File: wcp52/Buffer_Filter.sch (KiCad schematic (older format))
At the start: 18 parts, among them Q10 MMBT3904, Q11 BFR540, Q12 BFR540

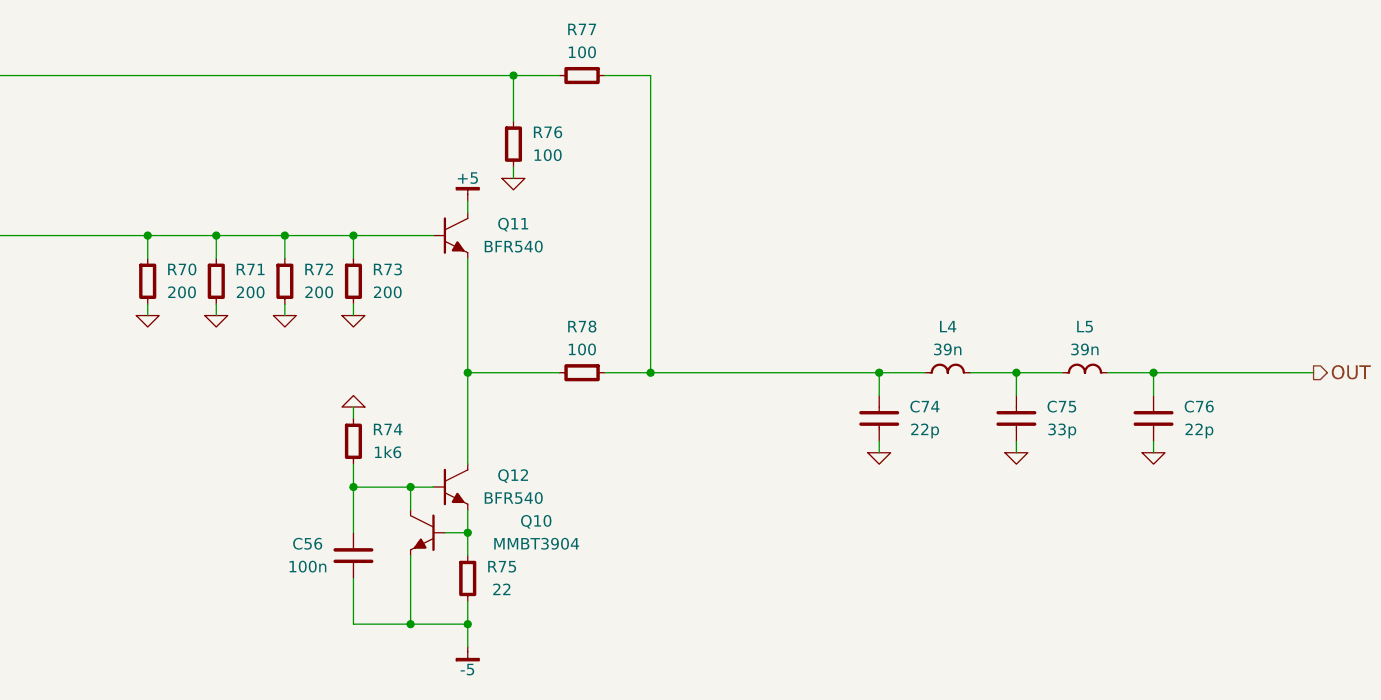
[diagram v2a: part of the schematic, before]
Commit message: Reannotate parts. May need to tweak silkscreen
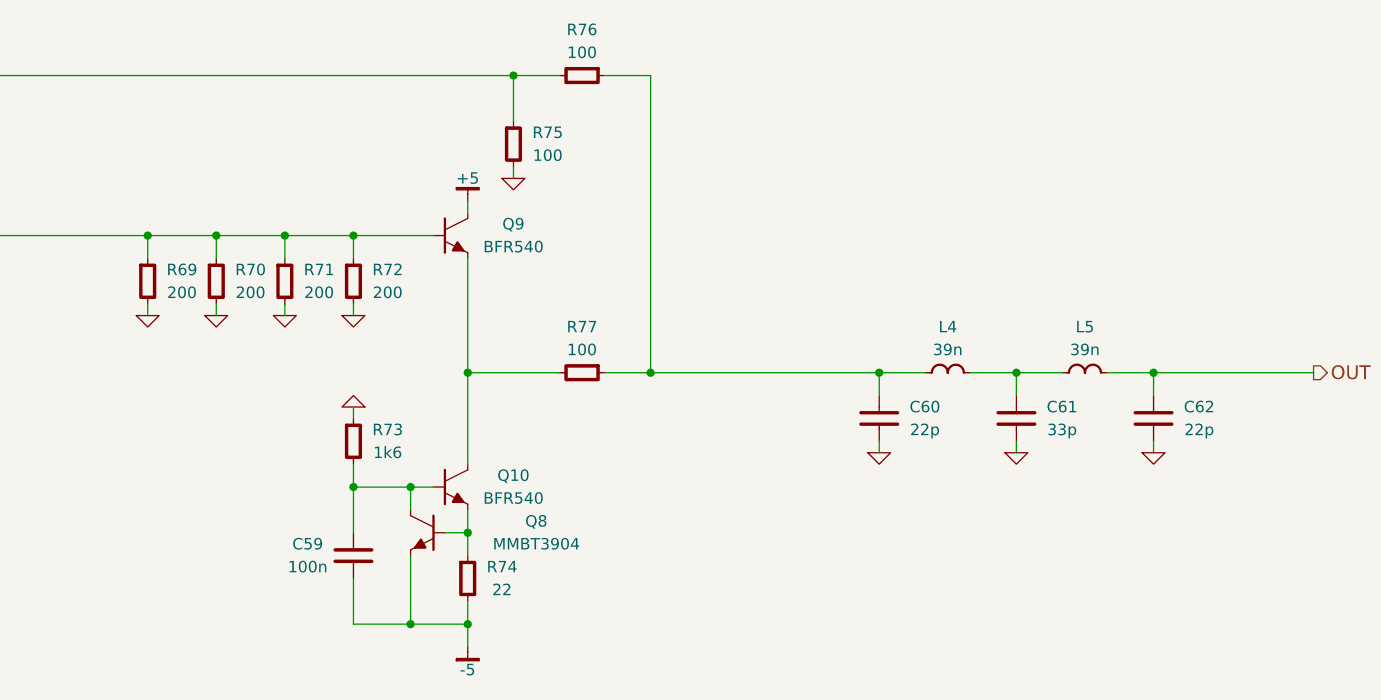
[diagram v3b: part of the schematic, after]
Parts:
- C59: renamed from C56; OldReference (none) -> C56
- C60: renamed from C74; OldReference (none) -> C74
- C61: renamed from C75; OldReference (none) -> C75
- C62: renamed from C76; OldReference (none) -> C76
- L4: OldReference (none) -> L4
- L5: OldReference (none) -> L5
- Q10: renamed from Q12; OldReference (none) -> Q12
- Q8: renamed from Q10; OldReference (none) -> Q10
- Q9: renamed from Q11; OldReference (none) -> Q11
- R69: renamed from R70; OldReference (none) -> R70
- R70: renamed from R71; OldReference (none) -> R71
- R71: renamed from R72; OldReference (none) -> R72
- R72: renamed from R73; OldReference (none) -> R73
- R73: renamed from R74; OldReference (none) -> R74
- R74: renamed from R75; OldReference (none) -> R75
- R75: renamed from R76; OldReference (none) -> R76
- R76: renamed from R77; OldReference (none) -> R77
- R77: renamed from R78; OldReference (none) -> R78
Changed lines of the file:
@@
 F 2 "" H 5200 2950 60  0000 C CNN
 F 3 "" H 5200 2950 60  0000 C CNN
+F 4 "#PWR0187" H 5200 2950 50  0001 C CNN "OldReference"
 	1    5200 2950
 	1    0    0    -1
@@
 F 2 "" H 5500 2950 60  0000 C CNN
 F 3 "" H 5500 2950 60  0000 C CNN
+F 4 "#PWR0188" H 5500 2950 50  0001 C CNN "OldReference"
 	1    5500 2950
 	1    0    0    -1
@@
 F 2 "" H 5800 2950 60  0000 C CNN
 F 3 "" H 5800 2950 60  0000 C CNN
+F 4 "#PWR0189" H 5800 2950 50  0001 C CNN "OldReference"
 	1    5800 2950
 	1    0    0    -1
@@
 F 2 "" H 6100 2950 60  0000 C CNN
 F 3 "" H 6100 2950 60  0000 C CNN
+F 4 "#PWR0190" H 6100 2950 50  0001 C CNN "OldReference"
 	1    6100 2950
 	1    0    0    -1
@@
 	6100 2950 6100 2900
 $Comp
-L BFR540 Q11
+L BFR540 Q9
 U 1 1 54F3761A
 P 6550 2600
-F 0 "Q11" H 6800 2650 50  0000 C CNN
+F 0 "Q9" H 6800 2650 50  0000 C CNN
 F 1 "BFR540" H 6800 2550 50  0000 C CNN
 F 2 "smd-semi:SOT-23" H 6550 2600 50  0001 C CNN
@@
 F 5 "DIST DIGIKEY 568-1649-1-ND" H 7300 3150 60  0001 C CNN "BOM"
 F 6 "NXP" H 6550 2600 60  0001 C CNN "Manuf"
+F 7 "Q11" H 6550 2600 50  0001 C CNN "OldReference"
 	1    6550 2600
 	1    0    0    -1
@@
 Connection ~ 5500 2600
 $Comp
-L BFR540 Q12
+L BFR540 Q10
 U 1 1 54F376D9
 P 6550 3700
-F 0 "Q12" H 6800 3750 50  0000 C CNN
+F 0 "Q10" H 6800 3750 50  0000 C CNN
 F 1 "BFR540" H 6800 3650 50  0000 C CNN
 F 2 "smd-semi:SOT-23" H 6550 3700 50  0001 C CNN
@@
 F 5 "DIST DIGIKEY 568-1649-1-ND" H 7300 4250 60  0001 C CNN "BOM"
 F 6 "NXP" H 6550 3700 60  0001 C CNN "Manuf"
+F 7 "Q12" H 6550 3700 50  0001 C CNN "OldReference"
 	1    6550 3700
 	1    0    0    -1
@@
 	6600 3600 6600 2700
 $Comp
-L MMBT3904 Q10
+L MMBT3904 Q8
 U 1 1 54F37ABD
 P 6400 3900
-F 0 "Q10" H 5900 3950 50  0000 C CNN
+F 0 "Q8" H 5900 3950 50  0000 C CNN
 F 1 "MMBT3904" H 5900 3850 50  0000 C CNN
 F 2 "smd-semi:SOT-23" H 6400 3900 50  0001 C CNN
@@
 F 4 "SEMI MMBT3904" H 7200 4450 60  0001 C CNN "BOM"
 F 5 "Value" H 6400 3900 60  0001 C CNN "Manuf"
+F 6 "Q10" H 6400 3900 50  0001 C CNN "OldReference"
 	1    6400 3900
 	-1   0    0    -1
@@
 F 2 "" H 6600 4400 60  0000 C CNN
 F 3 "" H 6600 4400 60  0000 C CNN
+F 4 "#PWR0191" H 6600 4400 50  0001 C CNN "OldReference"
 	1    6600 4400
 	1    0    0    -1
@@
 F 2 "" H 6100 3350 60  0000 C CNN
 F 3 "" H 6100 3350 60  0000 C CNN
+F 4 "#PWR0192" H 6100 3350 50  0001 C CNN "OldReference"
 	1    6100 3350
 	-1   0    0    1
@@
 F 2 "" H 6800 2350 60  0000 C CNN
 F 3 "" H 6800 2350 60  0000 C CNN
+F 4 "#PWR0193" H 6800 2350 50  0001 C CNN "OldReference"
 	1    6800 2350
 	1    0    0    -1
@@
 Connection ~ 7400 3200
 $Comp
-L C-0603 C74
+L C-0603 C60
 U 1 1 54F390B6
 P 8400 3400
-F 0 "C74" H 8600 3450 50  0000 C CNN
+F 0 "C60" H 8600 3450 50  0000 C CNN
 F 1 "22p" H 8600 3350 50  0000 C CNN
 F 2 "IPC7351-Nominal:CAPC1608X55" H 8400 3400 50  0001 C CNN
@@
 F 5 "TDK" H 8400 3400 60  0001 C CNN "Manuf"
 F 6 "DIST DIGIKEY 445-5366-1-ND" H 9200 3950 60  0001 C CNN "BOM"
+F 7 "C74" H 8400 3400 50  0001 C CNN "OldReference"
 	1    8400 3400
 	1    0    0    -1
@@
 F 2 "" H 8400 3550 60  0000 C CNN
 F 3 "" H 8400 3550 60  0000 C CNN
+F 4 "#PWR0194" H 8400 3550 50  0001 C CNN "OldReference"
 	1    8400 3550
 	1    0    0    -1
@@
 F 5 "Panasonic" H 8700 3200 60  0001 C CNN "Manuf"
 F 6 "DIST DIGIKEY PCD1917CT-ND" H 8700 3200 60  0001 C CNN "BOM"
+F 7 "L4" H 8700 3200 50  0001 C CNN "OldReference"
 	1    8700 3200
 	0    1    1    0
@@
 F 5 "Panasonic" H 9300 3200 60  0001 C CNN "Manuf"
 F 6 "DIST DIGIKEY PCD1917CT-ND" H 9300 3200 60  0001 C CNN "BOM"
+F 7 "L5" H 9300 3200 50  0001 C CNN "OldReference"
 	1    9300 3200
 	0    1    1    0
 $EndComp
 $Comp
-L C-0603 C75
+L C-0603 C61
 U 1 1 54F39A8A
 P 9000 3400
-F 0 "C75" H 9200 3450 50  0000 C CNN
+F 0 "C61" H 9200 3450 50  0000 C CNN
 F 1 "33p" H 9200 3350 50  0000 C CNN
 F 2 "IPC7351-Nominal:CAPC1608X55" H 9000 3400 50  0001 C CNN
@@
 F 5 "TDK" H 9000 3400 60  0001 C CNN "Manuf"
 F 6 "DIST DIGIKEY 445-7027-1-ND" H 9800 3950 60  0001 C CNN "BOM"
+F 7 "C75" H 9000 3400 50  0001 C CNN "OldReference"
 	1    9000 3400
 	1    0    0    -1
@@
 F 2 "" H 9000 3550 60  0000 C CNN
 F 3 "" H 9000 3550 60  0000 C CNN
+F 4 "#PWR0195" H 9000 3550 50  0001 C CNN "OldReference"
 	1    9000 3550
 	1    0    0    -1
@@
 	9000 3550 9000 3500
 $Comp
-L C-0603 C76
+L C-0603 C62
 U 1 1 54F39C2D
 P 9600 3400
-F 0 "C76" H 9800 3450 50  0000 C CNN
+F 0 "C62" H 9800 3450 50  0000 C CNN
 F 1 "22p" H 9800 3350 50  0000 C CNN
 F 2 "IPC7351-Nominal:CAPC1608X55" H 9600 3400 50  0001 C CNN
@@
 F 5 "TDK" H 9600 3400 60  0001 C CNN "Manuf"
 F 6 "DIST DIGIKEY 445-5366-1-ND" H 10400 3950 60  0001 C CNN "BOM"
+F 7 "C76" H 9600 3400 50  0001 C CNN "OldReference"
 	1    9600 3400
 	1    0    0    -1
@@
 F 2 "" H 9600 3550 60  0000 C CNN
 F 3 "" H 9600 3550 60  0000 C CNN
+F 4 "#PWR0196" H 9600 3550 50  0001 C CNN "OldReference"
 	1    9600 3550
 	1    0    0    -1
@@
 F 2 "" H 6600 2450 60  0000 C CNN
 F 3 "" H 6600 2450 60  0000 C CNN
+F 4 "#PWR0197" H 6600 2450 50  0001 C CNN "OldReference"
 	1    6600 2450
 	1    0    0    -1
@@
 	6600 2450 6600 2500
 $Comp
-L C-0603 C56
+L C-0603 C59
 U 1 1 54FF3F66
 P 6100 4000
-F 0 "C56" H 6300 4050 50  0000 C CNN
+F 0 "C59" H 6300 4050 50  0000 C CNN
 F 1 "100n" H 6300 3950 50  0000 C CNN
 F 2 "IPC7351-Nominal:CAPC1608X55" H 6100 4000 50  0001 C CNN
@@
 F 4 "Value" H 6100 4000 60  0001 C CNN "Manuf"
 F 5 "CAP MLCC 100n ≥X7R 16V 10% [0603]" H 6900 4550 60  0001 C CNN "BOM"
+F 6 "C56" H 6100 4000 50  0001 C CNN "OldReference"
 	1    6100 4000
 	-1   0    0    -1
 $EndComp
 $Comp
-L R-0603 R75
+L R-0603 R74
 U 1 1 5502993D
 P 6600 4100
-F 0 "R75" H 6750 4150 50  0000 C CNN
+F 0 "R74" H 6750 4150 50  0000 C CNN
 F 1 "22" H 6750 4050 50  0000 C CNN
 F 2 "IPC7351-Nominal:RESC1608X50" H 6600 4100 50  0001 C CNN
@@
 F 4 "Value" H 6600 4100 60  0001 C CNN "Manuf"
 F 5 "RES SMD 22 5% [0603]" H 7350 4650 60  0001 C CNN "BOM"
+F 6 "R75" H 6600 4100 50  0001 C CNN "OldReference"
 	1    6600 4100
 	1    0    0    -1
 $EndComp
 $Comp
-L R-0603 R74
+L R-0603 R73
 U 1 1 55029B6F
 P 6100 3500
-F 0 "R74" H 6250 3550 50  0000 C CNN
+F 0 "R73" H 6250 3550 50  0000 C CNN
 F 1 "1k6" H 6250 3450 50  0000 C CNN
 F 2 "IPC7351-Nominal:RESC1608X50" H 6100 3500 50  0001 C CNN
@@
 F 4 "Value" H 6100 3500 60  0001 C CNN "Manuf"
 F 5 "RES SMD 1.6k 1% [0603]" H 6850 4050 60  0001 C CNN "BOM"
+F 6 "R74" H 6100 3500 50  0001 C CNN "OldReference"
 	1    6100 3500
 	1    0    0    -1
 $EndComp
 $Comp
-L R-0603 R70
+L R-0603 R69
 U 1 1 5502BF89
 P 5200 2800
-F 0 "R70" H 5350 2850 50  0000 C CNN
+F 0 "R69" H 5350 2850 50  0000 C CNN
 F 1 "200" H 5350 2750 50  0000 C CNN
 F 2 "IPC7351-Nominal:RESC1608X50" H 5200 2800 50  0001 C CNN
@@
 F 4 "Value" H 5200 2800 60  0001 C CNN "Manuf"
 F 5 "RES SMD 200 1% [0603]" H 5950 3350 60  0001 C CNN "BOM"
+F 6 "R70" H 5200 2800 50  0001 C CNN "OldReference"
 	1    5200 2800
 	1    0    0    -1
 $EndComp
 $Comp
-L R-0603 R71
+L R-0603 R70
 U 1 1 5502C187
 P 5500 2800
-F 0 "R71" H 5650 2850 50  0000 C CNN
+F 0 "R70" H 5650 2850 50  0000 C CNN
 F 1 "200" H 5650 2750 50  0000 C CNN
 F 2 "IPC7351-Nominal:RESC1608X50" H 5500 2800 50  0001 C CNN
@@
 F 4 "Value" H 5500 2800 60  0001 C CNN "Manuf"
 F 5 "RES SMD 200 1% [0603]" H 6250 3350 60  0001 C CNN "BOM"
+F 6 "R71" H 5500 2800 50  0001 C CNN "OldReference"
 	1    5500 2800
 	1    0    0    -1
 $EndComp
 $Comp
-L R-0603 R72
+L R-0603 R71
 U 1 1 5502C1C3
 P 5800 2800
-F 0 "R72" H 5950 2850 50  0000 C CNN
+F 0 "R71" H 5950 2850 50  0000 C CNN
 F 1 "200" H 5950 2750 50  0000 C CNN
 F 2 "IPC7351-Nominal:RESC1608X50" H 5800 2800 50  0001 C CNN
@@
 F 4 "Value" H 5800 2800 60  0001 C CNN "Manuf"
 F 5 "RES SMD 200 1% [0603]" H 6550 3350 60  0001 C CNN "BOM"
+F 6 "R72" H 5800 2800 50  0001 C CNN "OldReference"
 	1    5800 2800
 	1    0    0    -1
 $EndComp
 $Comp
-L R-0603 R73
+L R-0603 R72
 U 1 1 5502C205
 P 6100 2800
-F 0 "R73" H 6250 2850 50  0000 C CNN
+F 0 "R72" H 6250 2850 50  0000 C CNN
 F 1 "200" H 6250 2750 50  0000 C CNN
 F 2 "IPC7351-Nominal:RESC1608X50" H 6100 2800 50  0001 C CNN
@@
 F 4 "Value" H 6100 2800 60  0001 C CNN "Manuf"
 F 5 "RES SMD 200 1% [0603]" H 6850 3350 60  0001 C CNN "BOM"
+F 6 "R73" H 6100 2800 50  0001 C CNN "OldReference"
 	1    6100 2800
 	1    0    0    -1
 $EndComp
 $Comp
-L R-0603 R77
+L R-0603 R76
 U 1 1 5502F5C9
 P 7100 1900
-F 0 "R77" V 6900 1900 50  0000 C CNN
+F 0 "R76" V 6900 1900 50  0000 C CNN
 F 1 "100" V 7000 1900 50  0000 C CNN
 F 2 "IPC7351-Nominal:RESC1608X50" H 7100 1900 50  0001 C CNN
@@
 F 4 "Value" H 7100 1900 60  0001 C CNN "Manuf"
 F 5 "RES SMD 100 1% [0603]" H 7850 2450 60  0001 C CNN "BOM"
+F 6 "R77" H 7100 1900 50  0001 C CNN "OldReference"
 	1    7100 1900
 	0    1    1    0
 $EndComp
 $Comp
-L R-0603 R76
+L R-0603 R75
 U 1 1 5502F7DE
 P 6800 2200
-F 0 "R76" H 6950 2250 50  0000 C CNN
+F 0 "R75" H 6950 2250 50  0000 C CNN
 F 1 "100" H 6950 2150 50  0000 C CNN
 F 2 "IPC7351-Nominal:RESC1608X50" H 6800 2200 50  0001 C CNN
@@
 F 4 "Value" H 6800 2200 60  0001 C CNN "Manuf"
 F 5 "RES SMD 100 1% [0603]" H 7550 2750 60  0001 C CNN "BOM"
+F 6 "R76" H 6800 2200 50  0001 C CNN "OldReference"
 	1    6800 2200
 	1    0    0    -1
 $EndComp
 $Comp
-L R-0603 R78
+L R-0603 R77
 U 1 1 5502F8BA
 P 7100 3200
-F 0 "R78" V 6900 3200 50  0000 C CNN
+F 0 "R77" V 6900 3200 50  0000 C CNN
 F 1 "100" V 7000 3200 50  0000 C CNN
 F 2 "IPC7351-Nominal:RESC1608X50" H 7100 3200 50  0001 C CNN
@@
 F 4 "Value" H 7100 3200 60  0001 C CNN "Manuf"
 F 5 "RES SMD 100 1% [0603]" H 7850 3750 60  0001 C CNN "BOM"
+F 6 "R78" H 7100 3200 50  0001 C CNN "OldReference"
 	1    7100 3200
 	0    1    1    0

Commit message: Schematic touchups
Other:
- note added: "Inside shield"
- note added: "Outside shield"
- moved on the sheet: C59, C60, C61, C62, L4, L5, Q10, Q8, Q9, R69, R70, R71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

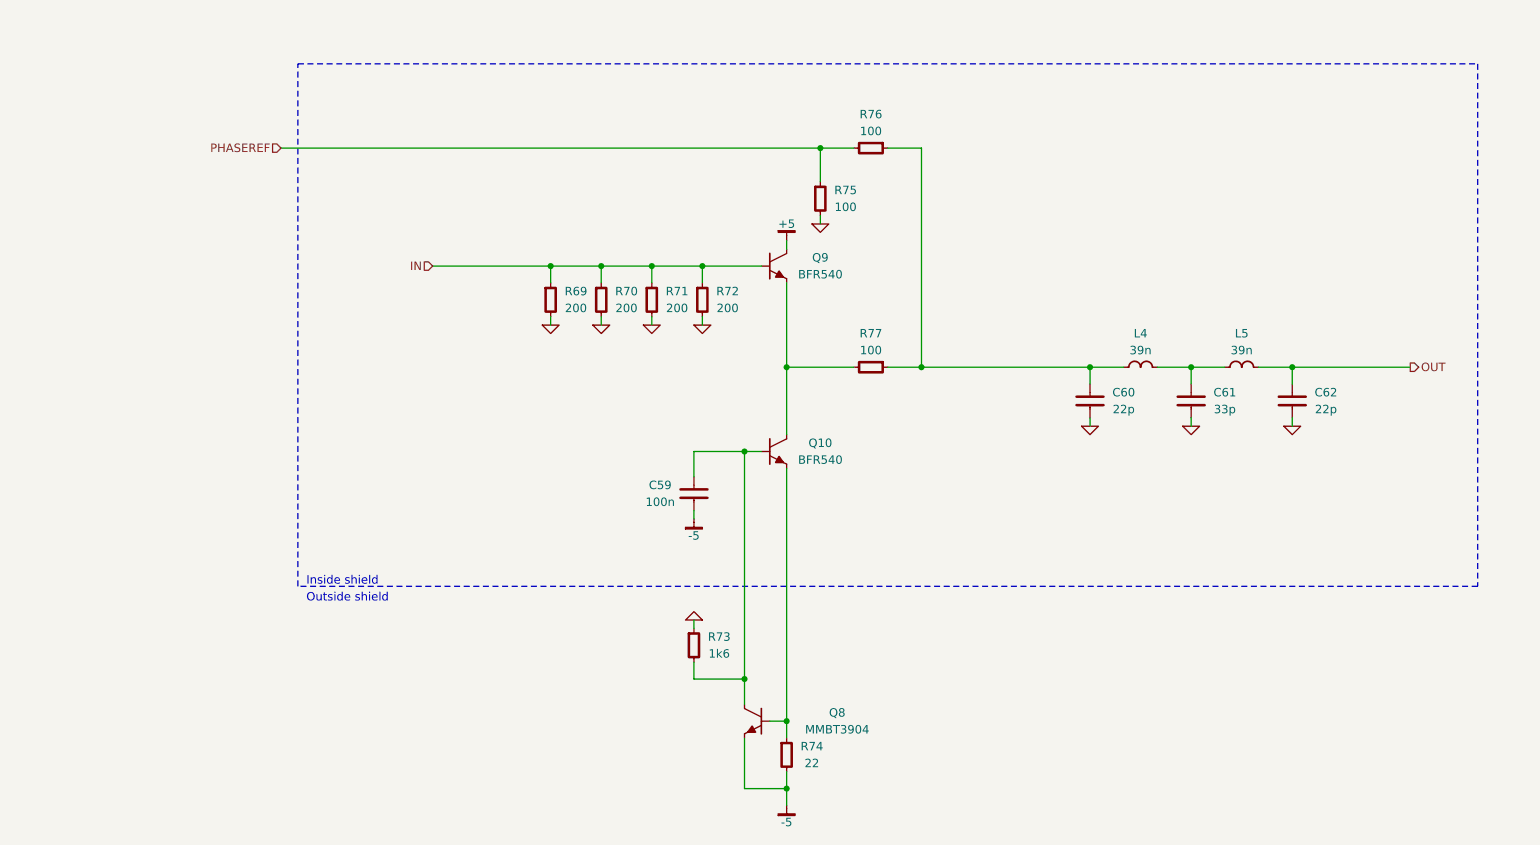
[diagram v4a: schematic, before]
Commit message: Change schematic pages to letter size
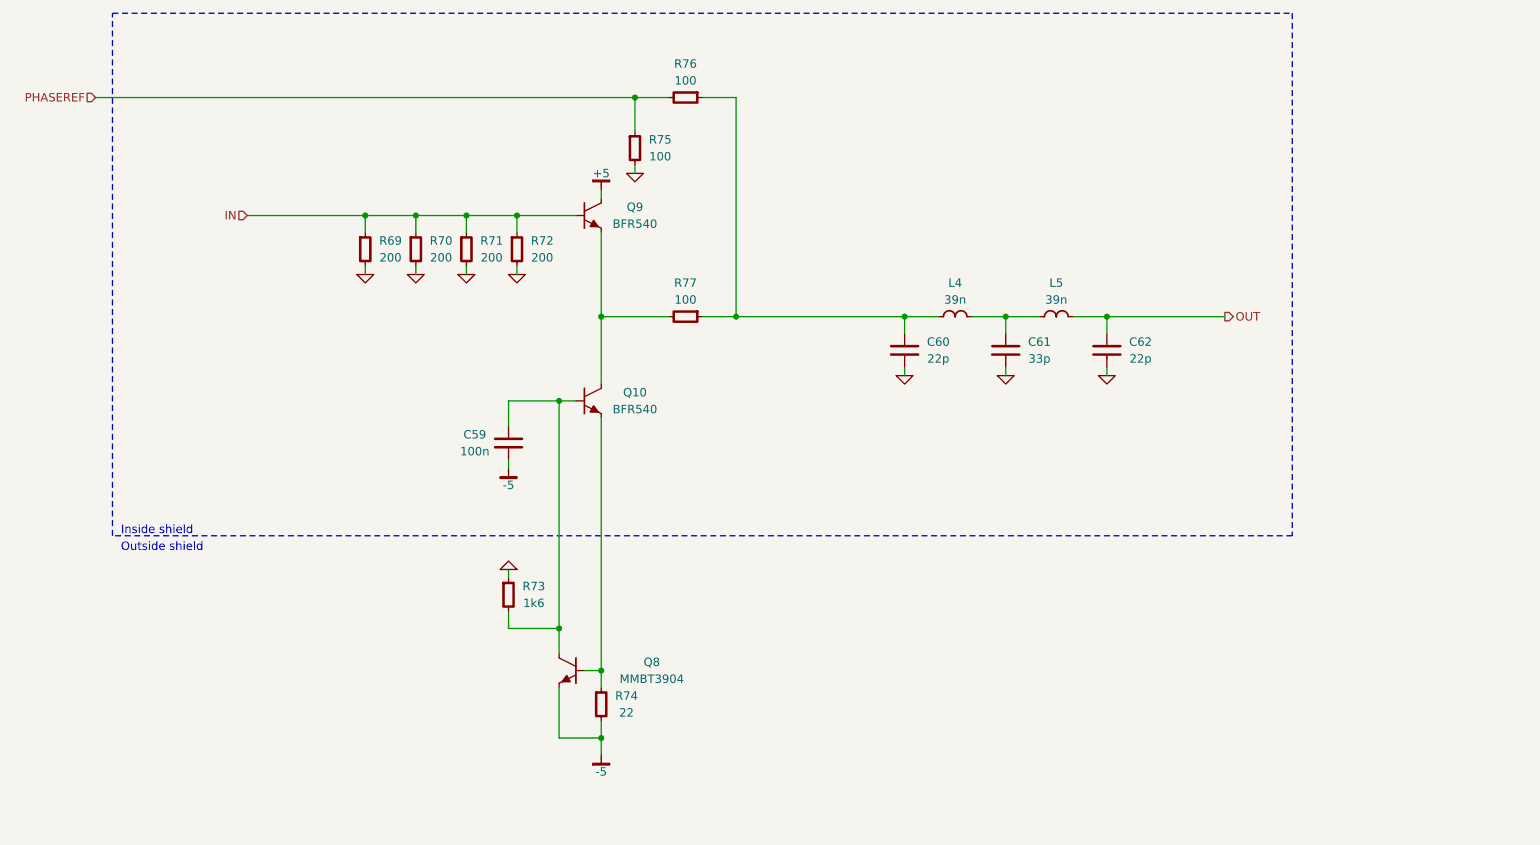
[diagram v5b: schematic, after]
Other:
- moved on the sheet: C59, C60, C61, C62, L4, L5, Q10, Q8, Q9, R69, R70, R71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

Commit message: BOM fixes
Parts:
- Q10, Q9: BOM DIST DIGIKEY 568-1649-1-ND -> SEMI NXP BFR540
- Q8: BOM SEMI MMBT3904 -> SEMI GENERIC MMBT3904
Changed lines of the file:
@@
 EESchema Schematic File Version 2
-LIBS:Altera
-LIBS:AnalogDevices
-LIBS:Atmel
-LIBS:conn-2mm
-LIBS:conn-100mil
-LIBS:conn-cui
-LIBS:conn-fci
-LIBS:conn-linx
-LIBS:conn-molex
-LIBS:conn-tagconnect
-LIBS:conn-test
-LIBS:DiodesInc
-LIBS:display
-LIBS:_electromech
-LIBS:Fairchild
-LIBS:FTDI
-LIBS:Intersil
-LIBS:Lattice
-LIBS:_linear
-LIBS:LinearTech
-LIBS:Littelfuse
-LIBS:logic-4000
-LIBS:logic-7400
-LIBS:MACOM
-LIBS:maxim
-LIBS:mechanical
-LIBS:Microchip
-LIBS:Micron
-LIBS:NXP
-LIBS:onsemi
-LIBS:passive
-LIBS:pasv-BiTech
-LIBS:pasv-Bourns
-LIBS:pasv-cap
-LIBS:pasv-ind
-LIBS:pasv-res
-LIBS:pcb
-LIBS:power
-LIBS:_semi
-LIBS:semi-diode-1N
-LIBS:semi-diode-BA
-LIBS:semi-diode-MCC
-LIBS:semi-diode-MMB
-LIBS:semi-diode-NXP
-LIBS:semi-diode-OnSemi
-LIBS:semi-diode-Vishay
-LIBS:semi-opto-misc
-LIBS:semi-thyristor-2N
-LIBS:semi-trans-2N
-LIBS:semi-trans-AO
-LIBS:semi-trans-BC
-LIBS:semi-trans-DiodesInc
-LIBS:semi-trans-Fairchild
-LIBS:semi-trans-Infineon
-LIBS:semi-trans-IntRect
-LIBS:semi-trans-IXYS
-LIBS:semi-trans-misc
-LIBS:semi-trans-MMB
-LIBS:semi-trans-MPS
-LIBS:semi-trans-NXP
-LIBS:semi-trans-PZT
-LIBS:semi-trans-TI
-LIBS:semi-trans-TIP
-LIBS:semi-trans-Toshiba
-LIBS:silabs
-LIBS:skyworks
-LIBS:ST
-LIBS:st_ic
-LIBS:st_semi
-LIBS:supertex
-LIBS:symbol
-LIBS:TexasInstruments
-LIBS:vishay_semi
-LIBS:Xilinx
-LIBS:pasv-xtal
-LIBS:conn-te
 LIBS:wcp52-cache
 EELAYER 25 0
@@
 F 3 "" H 5050 2600 60  0000 C CNN
 F 4 "BFR540,215" H 5400 2750 60  0001 C CNN "PN"
-F 5 "DIST DIGIKEY 568-1649-1-ND" H 5800 3150 60  0001 C CNN "BOM"
-F 6 "NXP" H 5050 2600 60  0001 C CNN "Manuf"
+F 5 "NXP" H 5050 2600 60  0001 C CNN "Manuf"
+F 6 "SEMI NXP BFR540" H 5800 3150 60  0001 C CNN "BOM"
 F 7 "Q11" H 5050 2600 50  0001 C CNN "OldReference"
 	1    5050 2600
@@
 F 3 "" H 5050 3700 60  0000 C CNN
 F 4 "BFR540,215" H 5400 3850 60  0001 C CNN "PN"
-F 5 "DIST DIGIKEY 568-1649-1-ND" H 5800 4250 60  0001 C CNN "BOM"
-F 6 "NXP" H 5050 3700 60  0001 C CNN "Manuf"
+F 5 "NXP" H 5050 3700 60  0001 C CNN "Manuf"
+F 6 "SEMI NXP BFR540" H 5800 4250 60  0001 C CNN "BOM"
 F 7 "Q12" H 5050 3700 50  0001 C CNN "OldReference"
 	1    5050 3700
@@
 F 2 "smd-semi:SOT-23" H 4900 5300 50  0001 C CNN
 F 3 "" H 4900 5300 60  0000 C CNN
-F 4 "SEMI MMBT3904" H 5700 5850 60  0001 C CNN "BOM"
-F 5 "Value" H 4900 5300 60  0001 C CNN "Manuf"
+F 4 "Value" H 4900 5300 60  0001 C CNN "Manuf"
+F 5 "SEMI GENERIC MMBT3904" H 5700 5850 60  0001 C CNN "BOM"
 F 6 "Q10" H 4900 5300 50  0001 C CNN "OldReference"
 	1    4900 5300
